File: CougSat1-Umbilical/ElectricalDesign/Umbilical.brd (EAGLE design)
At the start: 50 x 50 mm, 55 parts, among them J1 USB, J2 Umbilical, J3 5V input, Q1 CSD16406Q3, Q2 CSD16406Q3, U1 FT230XQ, U2 BQ24650

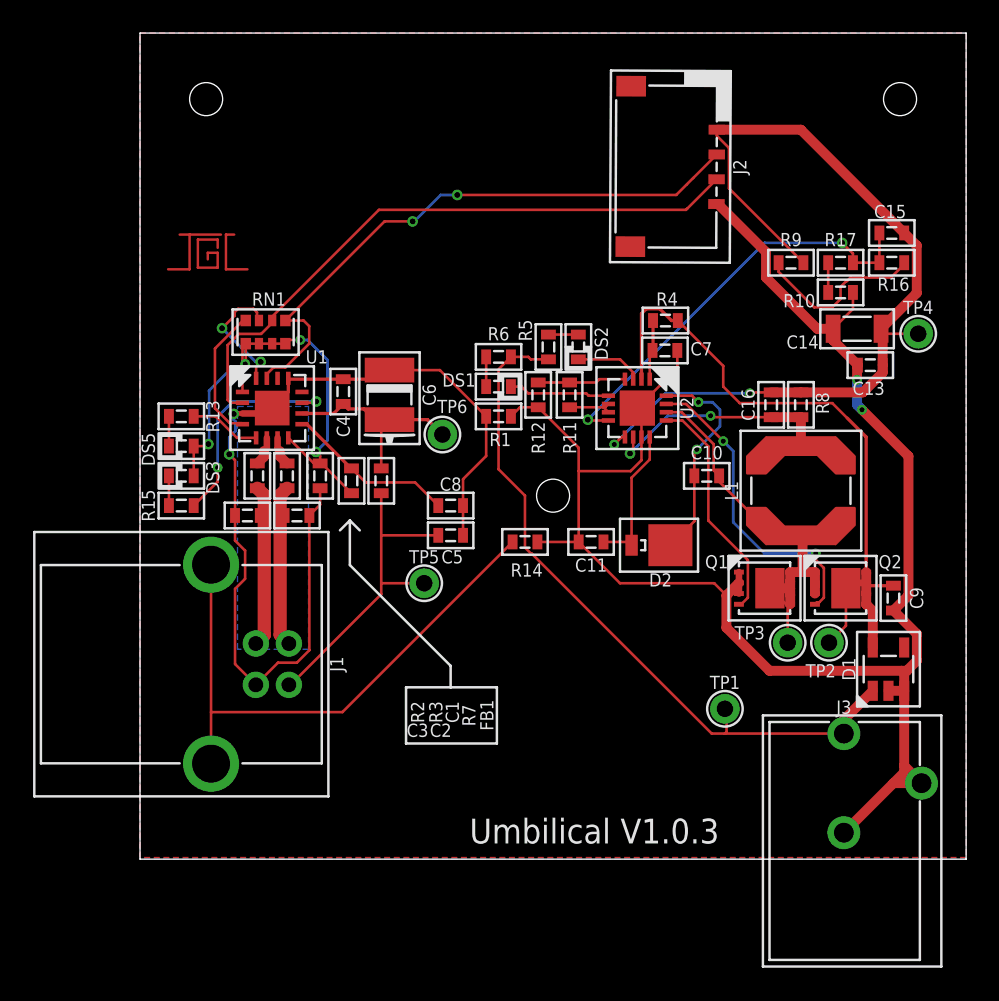
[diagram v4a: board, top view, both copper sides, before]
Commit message: Drew Mechanical Page
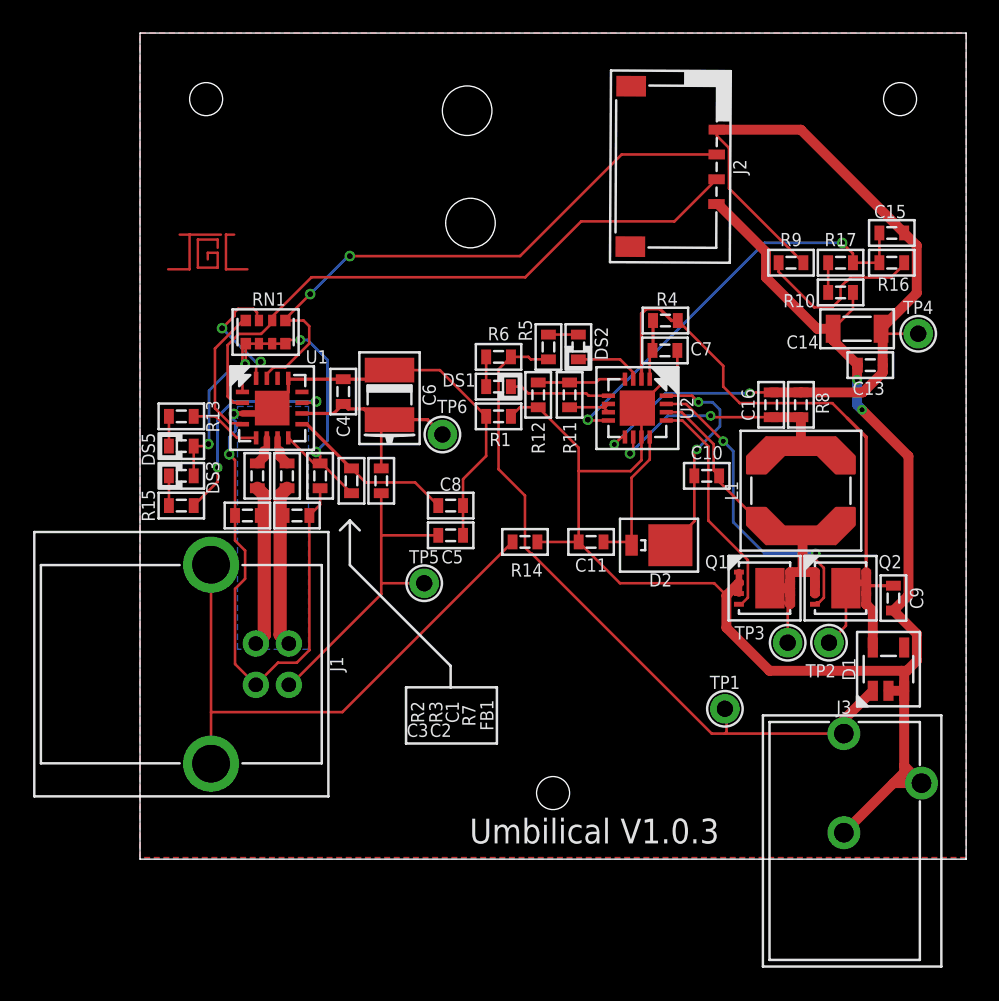
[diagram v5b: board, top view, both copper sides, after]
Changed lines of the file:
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@@
 <hole x="4" y="46" drill="2"/>
 <hole x="46" y="46" drill="2"/>
-<hole x="25" y="22" drill="2"/>
+<hole x="25" y="4" drill="2"/>
+<hole x="19.8" y="45.3" drill="3"/>
+<hole x="20" y="38.5" drill="3"/>
 </plain>
 <attributes>
@@
 <contactref element="U1" pad="15"/>
 <contactref element="RN1" pad="1"/>
-<wire x1="14.8" y1="38.6" x2="8.8" y2="32.6" width="0.16" layer="1"/>
 <wire x1="8.8" y1="32.6" x2="9.9" y2="32.6" width="0.16" layer="1"/>
 <wire x1="9.9" y1="32.6" x2="10.24" y2="32.26" width="0.16" layer="1"/>
@@
 <wire x1="8.07730625" y1="29.76" x2="8.79868125" y2="29.76" width="0.16" layer="1"/>
 <wire x1="8.79868125" y1="29.76" x2="10.24" y2="31.20131875" width="0.16" layer="1"/>
-<wire x1="34.903925" y1="42.6499875" x2="33.47696875" y2="41.22303125" width="0.16" layer="1"/>
-<wire x1="33.47696875" y1="41.22303125" x2="33.103925" y2="40.8499875" width="0.16" layer="1"/>
-<wire x1="16.5" y1="38.6" x2="16.6" y2="38.6" width="0.16" layer="16"/>
-<via x="16.5" y="38.6" extent="1-16" drill="0.35"/>
-<wire x1="16.5" y1="38.6" x2="14.8" y2="38.6" width="0.16" layer="1"/>
-<wire x1="18.2" y1="40.2" x2="19.2" y2="40.2" width="0.16" layer="16"/>
-<via x="19.2" y="40.2" extent="1-16" drill="0.35"/>
-<wire x1="19.2" y1="40.2" x2="32.4539375" y2="40.2" width="0.16" layer="1"/>
-<wire x1="32.4539375" y1="40.2" x2="33.103925" y2="40.8499875" width="0.16" layer="1"/>
-<wire x1="16.6" y1="38.6" x2="18.2" y2="40.2" width="0.16" layer="16"/>
+<via x="12.7" y="36.5" extent="1-16" drill="0.35"/>
+<wire x1="8.8" y1="32.7" x2="10.3" y2="34.2" width="0.16" layer="1"/>
+<wire x1="8.8" y1="32.6" x2="8.8" y2="32.7" width="0.16" layer="1"/>
+<via x="10.3" y="34.2" extent="1-16" drill="0.35"/>
+<wire x1="10.3" y1="34.2" x2="12.6" y2="36.5" width="0.16" layer="16"/>
+<wire x1="12.6" y1="36.5" x2="12.7" y2="36.5" width="0.16" layer="16"/>
+<wire x1="12.7" y1="36.5" x2="23" y2="36.5" width="0.16" layer="1"/>
+<wire x1="29.1499875" y1="42.6499875" x2="34.903925" y2="42.6499875" width="0.16" layer="1"/>
+<wire x1="23" y1="36.5" x2="29.1499875" y2="42.6499875" width="0.16" layer="1"/>
 </signal>
 <signal name="UMB_TX">
@@
 <contactref element="RN1" pad="2"/>
 <wire x1="8" y1="32.83769375" x2="8" y2="32.6" width="0.16" layer="1"/>
-<wire x1="14.46230625" y1="39.3" x2="8" y2="32.83769375" width="0.16" layer="1"/>
+<wire x1="10.381153125" y1="35.218846875" x2="8" y2="32.83769375" width="0.16" layer="1"/>
 <wire x1="7.3294125" y1="31.79" x2="8" y2="32.4605875" width="0.16" layer="1"/>
 <wire x1="5.9805875" y1="31.79" x2="7.3294125" y2="31.79" width="0.16" layer="1"/>
-<wire x1="6.2" y1="27.625" x2="5.9705875" y2="27.625" width="0.16" layer="1"/>
 <wire x1="8" y1="32.4605875" x2="8" y2="32.6" width="0.16" layer="1"/>
-<wire x1="6.2" y1="27.625" x2="5.475" y2="27.625" width="0.16" layer="1"/>
-<wire x1="5.475" y1="27.625" x2="5.3" y2="27.8" width="0.16" layer="1"/>
-<wire x1="5.3" y1="27.8" x2="5.3" y2="31.1094125" width="0.16" layer="1"/>
+<wire x1="5.3" y1="31.1094125" x2="5.3" y2="28" width="0.16" layer="1"/>
 <wire x1="5.3" y1="31.1094125" x2="5.9805875" y2="31.79" width="0.16" layer="1"/>
-<wire x1="34.896071875" y1="41.150009375" x2="33.12303125" y2="39.37696875" width="0.16" layer="1"/>
-<wire x1="33.12303125" y1="39.37696875" x2="33.0460625" y2="39.3" width="0.16" layer="1"/>
-<wire x1="33.0460625" y1="39.3" x2="14.46230625" y2="39.3" width="0.16" layer="1"/>
+<wire x1="34.896071875" y1="41.150009375" x2="32.3460625" y2="38.6" width="0.16" layer="1"/>
+<wire x1="23.318846875" y1="35.218846875" x2="10.381153125" y2="35.218846875" width="0.16" layer="1"/>
+<wire x1="32.3460625" y1="38.6" x2="26.7" y2="38.6" width="0.16" layer="1"/>
+<wire x1="26.7" y1="38.6" x2="23.318846875" y2="35.218846875" width="0.16" layer="1"/>
+<wire x1="5.3" y1="28" x2="5.675" y2="27.625" width="0.16" layer="1"/>
+<wire x1="5.675" y1="27.625" x2="6.2" y2="27.625" width="0.16" layer="1"/>
 </signal>
 <signal name="3.3V">

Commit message: Fixed The Last Issues
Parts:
- added H1, H2, H3: M3, CougsInSpace-Hardware:MOUNTING_HOLE-3.3
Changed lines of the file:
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@@
 <wire x1="50" y1="50" x2="0" y2="50" width="0" layer="20"/>
 <wire x1="0" y1="50" x2="0" y2="0" width="0" layer="20"/>
-<text x="27.5" y="1.7" size="1.5" layer="21" font="vector" ratio="15" rot="R180" align="center">Umbilical V1.0.3</text>
+<text x="14.1" y="1.4" size="1.5" layer="21" font="vector" ratio="15" rot="R180" align="center">Umbilical V1.0.3</text>
 <wire x1="16.1" y1="10.4" x2="16.1" y2="7" width="0.1524" layer="21"/>
 <wire x1="16.1" y1="7" x2="21.6" y2="7" width="0.1524" layer="21"/>
@@
 <wire x1="12.7" y1="20.5" x2="13.3" y2="19.9" width="0.1524" layer="21"/>
 <wire x1="12.7" y1="20.5" x2="12.1" y2="19.9" width="0.1524" layer="21"/>
-<hole x="4" y="46" drill="2"/>
-<hole x="46" y="46" drill="2"/>
-<hole x="25" y="4" drill="2"/>
 <hole x="19.8" y="45.3" drill="3"/>
 <hole x="20" y="38.5" drill="3"/>
@@
 </element>
 <element name="LOGO1" library="CougsInSpace-Aesthetics" package="SIGN-JAYSON" value="SIGNATUREJAYSON" x="4.1" y="36.7" smashed="yes"/>
+<element name="H1" library="CougsInSpace-Hardware" package="MOUNTING_HOLE-3.3" value="M3" x="45" y="45" smashed="yes">
+<attribute name="NAME" x="45" y="49" size="0.8" layer="25" font="vector" ratio="15" align="center"/>
+<attribute name="SKU" value="48-004x" x="45" y="45" size="1.778" layer="27" display="off"/>
+</element>
+<element name="H2" library="CougsInSpace-Hardware" package="MOUNTING_HOLE-3.3" value="M3" x="5" y="45" smashed="yes">
+<attribute name="NAME" x="5" y="49" size="0.8" layer="25" font="vector" ratio="15" align="center"/>
+<attribute name="SKU" value="48-004x" x="5" y="45" size="1.778" layer="27" display="off"/>
+</element>
+<element name="H3" library="CougsInSpace-Hardware" package="MOUNTING_HOLE-3.3" value="M3" x="25" y="5" smashed="yes">
+<attribute name="NAME" x="25" y="9" size="0.8" layer="25" font="vector" ratio="15" align="center"/>
+<attribute name="SKU" value="48-004x" x="25" y="5" size="1.778" layer="27" display="off"/>
+</element>
 </elements>
 <signals>
